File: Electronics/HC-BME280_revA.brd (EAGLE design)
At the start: 100 x 80 mm, 18 parts, among them T2 AO3401, U1 ATMEGA328-20P, U2 NRF24L01, U3 BME280, U4 OLED128X64

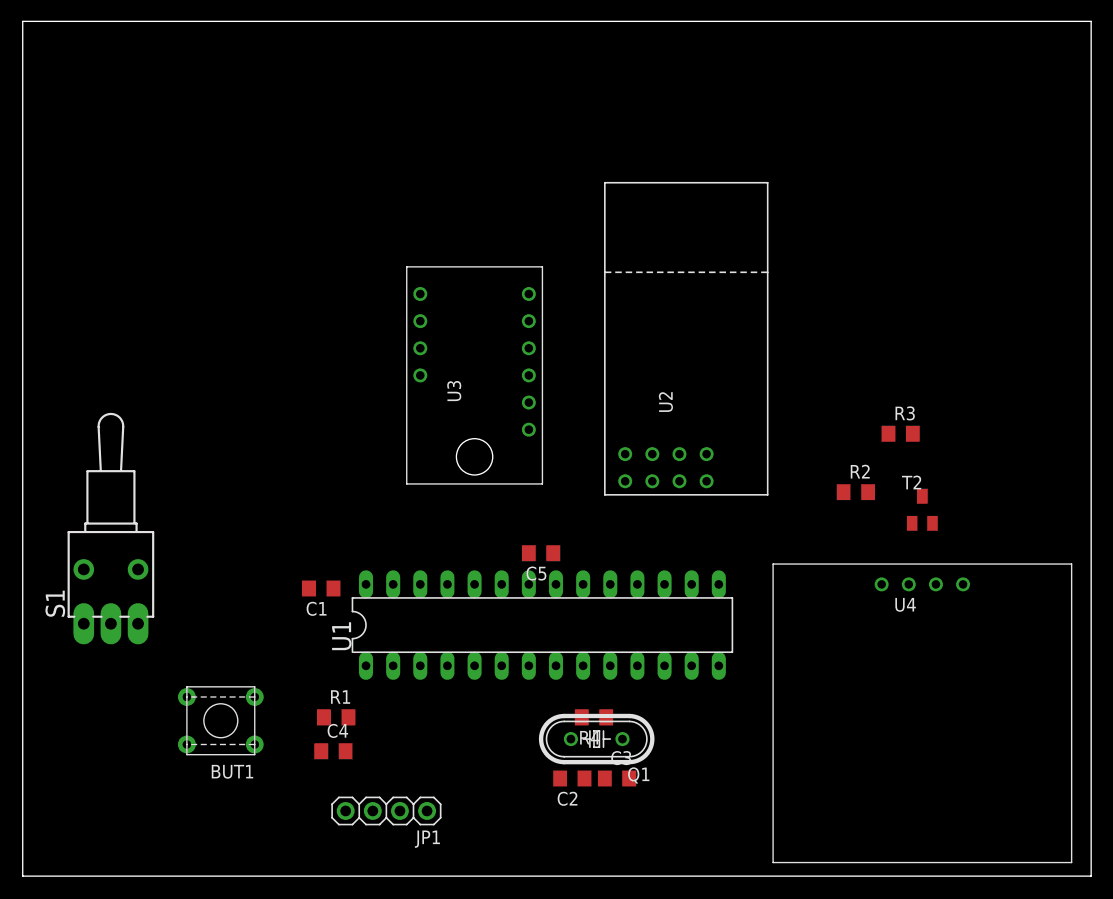
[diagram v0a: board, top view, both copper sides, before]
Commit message: modified: diagram and PCB
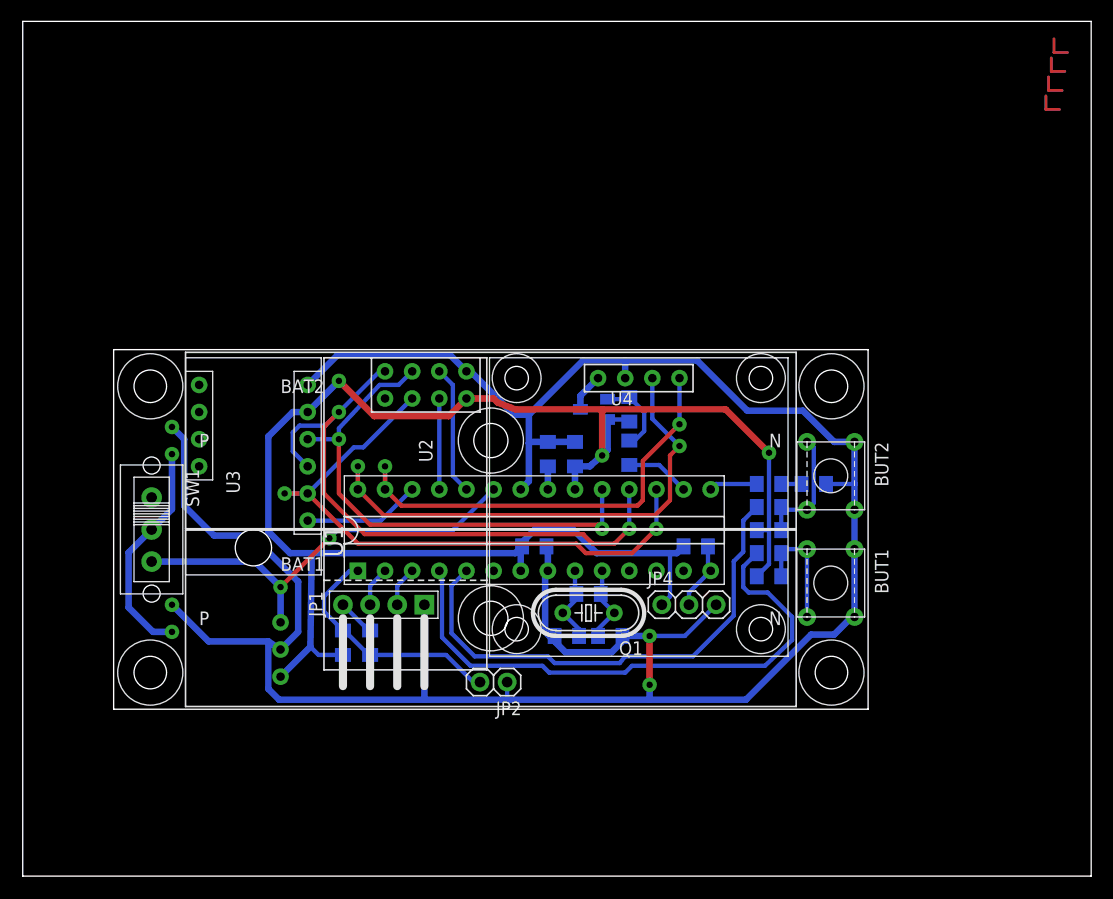
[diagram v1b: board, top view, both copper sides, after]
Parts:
- removed S1: (no value), 1_domaci:TL3XWO
- added BAT1, BAT2: 1V5, 1_domaci:1XAA_BATTERY_HOLDER
- added BUT2: BUTTON'THT', 1_domaci:BUTTON
- added C6: 100n, 1_domaci:C0805
- added JP2: PINHD-2X1, 1_domaci:PINHD-2X1
- added JP4: PINHD-3X1, 1_domaci:PINHD-3X1
- added LED1: (no value), 1_domaci:LED0805
- added R10: 4K7, 1_domaci:R0805
- added R5, R7: 10K, 1_domaci:R0805
- added R6, R8: 220R, 1_domaci:R0805
- added R9: 1K, 1_domaci:R0805
- added SW1: SWITCH_SLIDE, 1_domaci:SLIDE_SWITCH
- added U$1, U$2, U$3, U$4: CORNER, 1_domaci:CORNER
- added U$5, U$6, U$7, U$8: HOLE, 1_domaci:HOLE
- added U5: BCO35, 1_domaci:BCO35
- JP1: device 1_domaci:1X04 -> 1_domaci:PINHD-4X1-90
- moved BUT1 58.4 mm to (75.9, 28.1), turned to 270 degrees
- moved U4 32.8 mm to (57.7, 46.6)
- moved T2 32.1 mm to (53.5, 43.7), flipped to the bottom, turned to 270 degrees
- moved U2 26.2 mm to (36.4, 46.0), turned to 270 degrees
- moved R3 25.5 mm to (56.8, 43.7), flipped to the bottom, turned to 270 degrees
- moved U3 22.4 mm to (21.6, 38.4)
- moved R2 21.5 mm to (56.8, 39.6), flipped to the bottom, turned to 270 degrees
- moved C1 20.3 mm to (47.9, 30.9), flipped to the bottom, turned to 0 degrees
- moved JP1 19.3 mm to (33.8, 25.4)
- moved C3 13.4 mm to (55.0, 22.5), flipped to the bottom
- moved C2 13.3 mm to (50.9, 22.5), flipped to the bottom
- moved Q1 11.8 mm to (53.0, 24.6)
- moved R4 11.6 mm to (53.0, 26.4), flipped to the bottom, turned to 0 degrees
- moved C4 10.7 mm to (32.5, 21.8), flipped to the bottom, turned to 90 degrees
- moved C5 9.29 mm to (49.1, 39.5), flipped to the bottom, turned to 90 degrees
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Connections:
- removed net !OLED_ENABLED: R2.2
- removed net AGND: C5.2, U1.22
- new net !OLED_EN: R2.2, U1.16
- new net BUT1: R6.1, U1.4
- new net BUT2: R8.1, U1.5
- new net CE_R: U1.24, U2.2
- new net CS_R: U1.25, U2.7
- new net CS_S: U1.26, U3.5
- new net DS18B20_1: JP4.2, R10.1, U1.14
- new net LED: R9.2, U1.15
- new net N$10: BUT2.1, BUT2.3, R7.1, R8.2
- new net N$11: LED1.1, R9.1
- new net N$8: BAT1.P, BAT2.P, SW1.2
- new net N$9: BUT1.1, BUT1.3, R5.1, R6.2
- new net VCC: U3.2
- new net V_BAT: SW1.3, U1.23, U5.IN
- net +3V3: now also C6.2, JP4.1, R10.2, R5.2, R7.2, U5.OUT; no longer U3.2
- net GND: now also BAT1.N, BAT2.N, BUT2.2, BUT2.4, C5.2, C6.1, JP2.1, JP4.3, LED1.2, U1.22, U5.GND
- net N$2: now also JP2.2; no longer BUT1.1, BUT1.3
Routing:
- net GND: track 0.00 -> 239.6 mm, vias 0 -> 2
- net +3V3: track 0.00 -> 156.0 mm, vias 0 -> 3
- net MISO: track 0.00 -> 57.7 mm, vias 0 -> 2
- net MOSI: track 0.00 -> 57.4 mm, vias 0 -> 2
- net BUT1: track 0.00 -> 53.3 mm
- net SCL: track 0.00 -> 48.0 mm, vias 0 -> 2
- net SCK: track 0.00 -> 47.9 mm, vias 0 -> 2
- net BUT2: track 0.00 -> 46.9 mm
- net SDA: track 0.00 -> 42.1 mm, vias 0 -> 2
- net V_BAT: track 0.00 -> 40.1 mm, vias 0 -> 2
- net N$2: track 0.00 -> 22.9 mm
- net N$8: track 0.00 -> 21.0 mm
- net CE_R: track 0.00 -> 12.1 mm
- net N$10: track 0.00 -> 11.6 mm
- net CS_S: track 0.00 -> 11.1 mm
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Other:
- outline, holes or cut-outs redrawn

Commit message: modified: PCB
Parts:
- moved U$2 122.2 mm to (0.64, 0.64)
- moved U$3 104.5 mm to (0.64, 33.0), turned to 270 degrees
- moved U$4 76.5 mm to (70.0, 0.64), turned to 90 degrees
- moved U$1 52.3 mm to (70.0, 33.0), turned to 180 degrees
- moved JP2 28.3 mm to (17.7, 7.87), turned to 90 degrees
- moved R6 19.7 mm to (61.3, 12.4)
- moved Q1 18.2 mm to (44.5, 8.51)
- moved C4 18.2 mm to (17.7, 11.3), turned to 180 degrees
- moved SW1 17.8 mm to (3.43, 16.9)
- moved BAT2 17.8 mm to (35.3, 25.1)
- moved BUT2 17.8 mm to (67.4, 22.5)
- moved R2 17.8 mm to (48.3, 24.0)
- moved R3 17.8 mm to (48.3, 28.1)
- moved T2 17.8 mm to (45.0, 28.1)
- moved U$7 17.8 mm to (3.43, 30.2)
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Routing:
- net +3V3: track 156.0 -> 131.8 mm
- net GND: track 239.6 -> 255.2 mm
- net N$2: track 22.9 -> 10.1 mm
- net SCL: track 48.0 -> 60.1 mm
- net BUT1: track 53.3 -> 42.8 mm
- net SDA: track 42.1 -> 50.8 mm
- net LED: track 4.53 -> 12.6 mm
- net N$8: track 21.0 -> 25.3 mm
- net SCK: track 47.9 -> 46.1 mm
- net DS18B20_1: track 6.41 -> 7.67 mm
- net MISO: track 57.7 -> 58.6 mm
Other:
- board size 100 x 80 mm -> 70.6 x 33.7 mm

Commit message: modified: PCB - revA
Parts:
- moved C4 6.25 mm to (21.5, 6.35), turned to 90 degrees
- moved U5 4.44 mm to (15.6, 6.86), flipped to the top, turned to 90 degrees
- moved LED1 2.03 mm to (67.6, 22.0)
- moved R1 1.97 mm to (19.6, 13.0)
- moved JP2 1.20 mm to (18.3, 6.86)
- moved JP4 0.25 mm to (54.7, 9.53)
- moved R2 0.13 mm to (48.3, 23.9)
- moved R3 0.13 mm to (48.3, 27.9)
- moved T2 0.13 mm to (45.0, 27.9)
- flipped BAT1 to the bottom, turned to 180 degrees
- flipped BAT2 to the bottom, turned to 180 degrees
- renumbered JP1 to JP3
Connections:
- net GND: now also JP3.4; no longer JP3.1
- net N$6: now also JP3.1; no longer JP3.4
- net RX: now also JP3.2; no longer JP3.3
- net TX: now also JP3.3; no longer JP3.2
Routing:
- net V_BAT: track 40.6 -> 51.5 mm
- net GND: track 255.2 -> 264.9 mm
- net N$2: track 10.1 -> 12.9 mm
- net N$10: track 11.6 -> 14.0 mm
- net N$11: track 1.90 -> 3.94 mm
- net BUT1: track 42.8 -> 44.3 mm
- net BUT2: track 46.8 -> 48.2 mm
- net N$6: track 3.30 -> 2.29 mm

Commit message: modified: minor changes in schematics and PCB
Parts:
- JP2: value PINHD-2X1 -> PINHD2X1
- JP3: value (none) -> PINHD3X1
- LED1: value (none) -> green
- Q1: value (none) -> 16MHz
- R1: value (none) -> 4k7
